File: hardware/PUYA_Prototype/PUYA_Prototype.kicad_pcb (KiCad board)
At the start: 2 copper layers, 19.3 x 31.8 mm, 26 parts, among them J1 SWD, J2 L_Terminal, J3 R_Terminal, SW1 SW_RST, U1 PY32F002AA15M6TU, U2 AP2112K-3.3TRG1

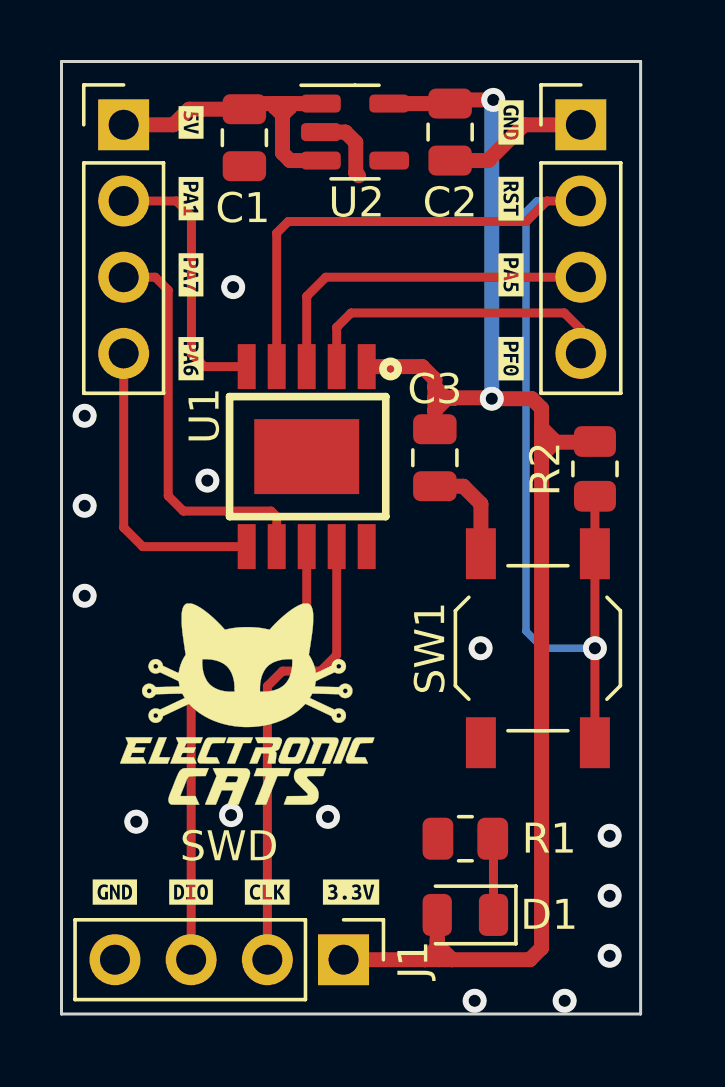
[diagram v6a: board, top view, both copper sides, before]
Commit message: change edge cuts
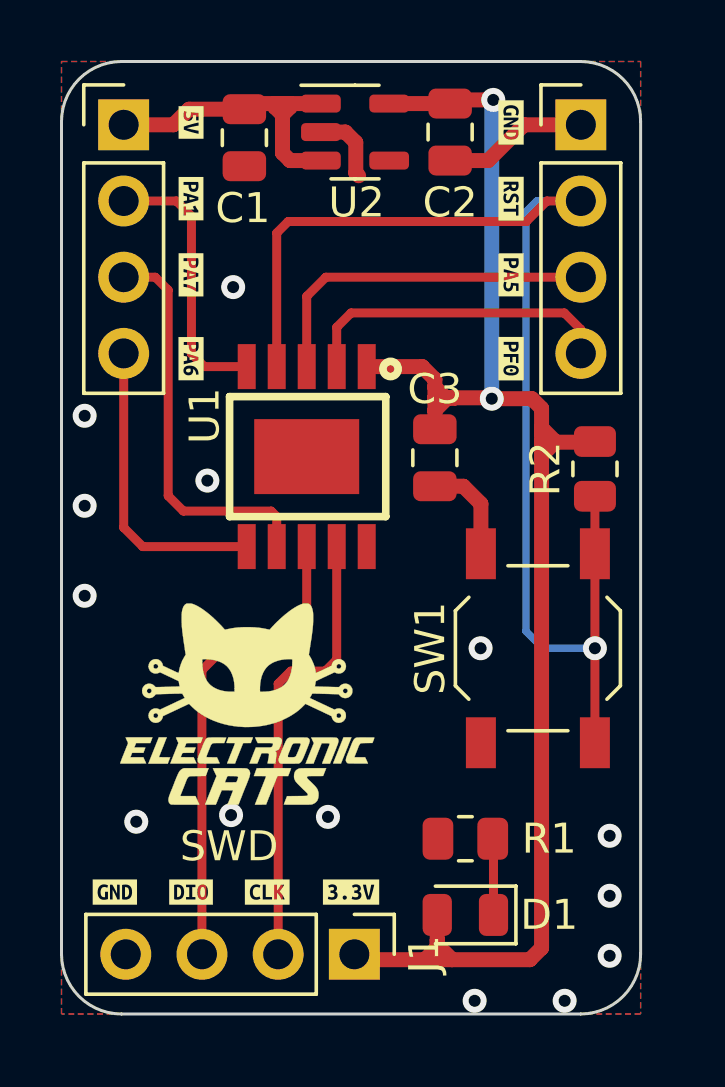
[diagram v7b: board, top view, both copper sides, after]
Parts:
- moved J1 0.40 mm to (119.5, 89.5)
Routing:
- net /SWDIO: track 17.1 -> 16.5 mm
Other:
- outline, holes or cut-outs redrawn
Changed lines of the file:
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@@
   )
   (footprint "Connector_PinHeader_2.54mm:PinHeader_1x04_P2.54mm_Vertical" (layer "F.Cu")
-    (at 119.13 89.63 -90)
+    (at 119.49 89.45 -90)
     (descr "Through hole straight pin header, 1x04, 2.54mm pitch, single row")
     (tags "Through hole pin header THT 1x04 2.54mm single row")
@@
       (stroke (width 0.01) (type solid)) (fill solid) (layer "B.SilkS"))
   )
-  (gr_rect (start 109.728 59.69) (end 129.032 91.44)
-    (stroke (width 0.1) (type default)) (fill none) (layer "Edge.Cuts"))
+  (gr_arc (start 111.728 91.44) (mid 110.313786 90.854214) (end 109.728 89.44)
+    (stroke (width 0.1) (type default)) (layer "Edge.Cuts"))
+  (gr_arc (start 127.032 59.69) (mid 128.446214 60.275786) (end 129.032 61.69)
+    (stroke (width 0.1) (type default)) (layer "Edge.Cuts"))
+  (gr_line (start 127.032 91.44) (end 111.728 91.44)
+    (stroke (width 0.1) (type default)) (layer "Edge.Cuts"))
+  (gr_arc (start 109.728 61.69) (mid 110.313786 60.275786) (end 111.728 59.69)
+    (stroke (width 0.1) (type default)) (layer "Edge.Cuts"))
+  (gr_line (start 111.728 59.69) (end 127.032 59.69)
+    (stroke (width 0.1) (type default)) (layer "Edge.Cuts"))
+  (gr_line (start 129.032 61.69) (end 129.032 89.44)
+    (stroke (width 0.1) (type default)) (layer "Edge.Cuts"))
+  (gr_arc (start 129.032 89.44) (mid 128.446214 90.854214) (end 127.032 91.44)
+    (stroke (width 0.1) (type default)) (layer "Edge.Cuts"))
+  (gr_line (start 109.728 89.44) (end 109.728 61.69)
+    (stroke (width 0.1) (type default)) (layer "Edge.Cuts"))
   (gr_text "Dev Board PY32F" (at 124.46 76.75) (layer "B.SilkS")
     (effects (font (size 1 1) (thickness 0.15)) (justify left bottom mirror))
@@
   (segment (start 122.2525 88.97) (end 122.2525 89.2175) (width 0.5) (layer "F.Cu") (net 3))
   (segment (start 121.75 69.860006) (end 119.901998 69.860006) (width 0.5) (layer "F.Cu") (net 3))
+  (segment (start 119.67 89.63) (end 121.84 89.63) (width 0.5) (layer "F.Cu") (net 3))
   (segment (start 127.4875 72.38) (end 127.51 72.3575) (width 0.5) (layer "F.Cu") (net 3))
   (segment (start 122.86 70.9) (end 122.594 70.9) (width 0.5) (layer "F.Cu") (net 3))
@@
   (segment (start 125.73 72.87) (end 125.73 72.38) (width 0.5) (layer "F.Cu") (net 3))
   (segment (start 126.18 72.35) (end 125.73 71.9) (width 0.5) (layer "F.Cu") (net 3))
+  (segment (start 119.49 89.45) (end 119.67 89.63) (width 0.5) (layer "F.Cu") (net 3))
   (segment (start 125.73 72.38) (end 126.18 72.38) (width 0.5) (layer "F.Cu") (net 3))
   (segment (start 122.174 70.9) (end 122.174 70.54) (width 0.5) (layer "F.Cu") (net 3))
@@
   (segment (start 122.174 70.9) (end 122.86 70.9) (width 0.5) (layer "F.Cu") (net 3))
   (segment (start 122.804 60.97) (end 124.12 60.97) (width 0.5) (layer "F.Cu") (net 3))
-  (segment (start 119.126 89.63) (end 121.84 89.63) (width 0.5) (layer "F.Cu") (net 3))
   (segment (start 122.2525 89.1325) (end 122.75 89.63) (width 0.5) (layer "F.Cu") (net 3))
   (segment (start 122.2525 89.2175) (end 121.84 89.63) (width 0.5) (layer "F.Cu") (net 3))
@@
   (segment (start 124.1025 85.598) (end 124.1275 85.623) (width 0.3) (layer "F.Cu") (net 4))
   (segment (start 124.1275 85.623) (end 124.1275 88.138) (width 0.3) (layer "F.Cu") (net 4))
-  (segment (start 117.094 80.01) (end 116.59 80.514) (width 0.3) (layer "F.Cu") (net 5))
-  (segment (start 118.364 80.01) (end 117.094 80.01) (width 0.3) (layer "F.Cu") (net 5))
-  (segment (start 116.59 89.658) (end 116.586 89.662) (width 0.3) (layer "F.Cu") (net 5))
-  (segment (start 118.902 75.859994) (end 118.902 79.472) (width 0.3) (layer "F.Cu") (net 5))
-  (segment (start 116.59 80.514) (end 116.59 89.658) (width 0.3) (layer "F.Cu") (net 5))
-  (segment (start 118.902 79.472) (end 118.364 80.01) (width 0.3) (layer "F.Cu") (net 5))
-  (segment (start 114.05 79.752) (end 114.05 89.658) (width 0.3) (layer "F.Cu") (net 6))
-  (segment (start 114.05 89.658) (end 114.046 89.662) (width 0.3) (layer "F.Cu") (net 6))
-  (segment (start 117.902002 78.693998) (end 117.348 79.248) (width 0.3) (layer "F.Cu") (net 6))
-  (segment (start 117.348 79.248) (end 114.554 79.248) (width 0.3) (layer "F.Cu") (net 6))
+  (segment (start 116.95 80.43) (end 116.95 89.45) (width 0.3) (layer "F.Cu") (net 5))
+  (segment (start 118.902 79.628) (end 118.52 80.01) (width 0.3) (layer "F.Cu") (net 5))
+  (segment (start 118.52 80.01) (end 117.37 80.01) (width 0.3) (layer "F.Cu") (net 5))
+  (segment (start 117.37 80.01) (end 116.95 80.43) (width 0.3) (layer "F.Cu") (net 5))
+  (segment (start 118.902 75.859994) (end 118.902 79.628) (width 0.3) (layer "F.Cu") (net 5))
+  (segment (start 114.41 79.98) (end 114.41 89.45) (width 0.3) (layer "F.Cu") (net 6))
+  (segment (start 117.902002 75.859994) (end 117.902002 78.927998) (width 0.3) (layer "F.Cu") (net 6))
   (segment (start 117.85 75.911996) (end 117.902002 75.859994) (width 0.3) (layer "F.Cu") (net 6))
-  (segment (start 114.554 79.248) (end 114.05 79.752) (width 0.3) (layer "F.Cu") (net 6))
-  (segment (start 117.902002 75.859994) (end 117.902002 78.693998) (width 0.3) (layer "F.Cu") (net 6))
+  (segment (start 117.38 79.45) (end 114.94 79.45) (width 0.3) (layer "F.Cu") (net 6))
+  (segment (start 117.902002 78.927998) (end 117.38 79.45) (width 0.3) (layer "F.Cu") (net 6))
+  (segment (start 114.94 79.45) (end 114.41 79.98) (width 0.3) (layer "F.Cu") (net 6))
   (segment (start 125.906 64.34) (end 127.04 64.34) (width 0.3) (layer "F.Cu") (net 7))
   (segment (start 125.222 65.024) (end 125.906 64.34) (width 0.3) (layer "F.Cu") (net 7))

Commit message: add "on" serigraphy to D1
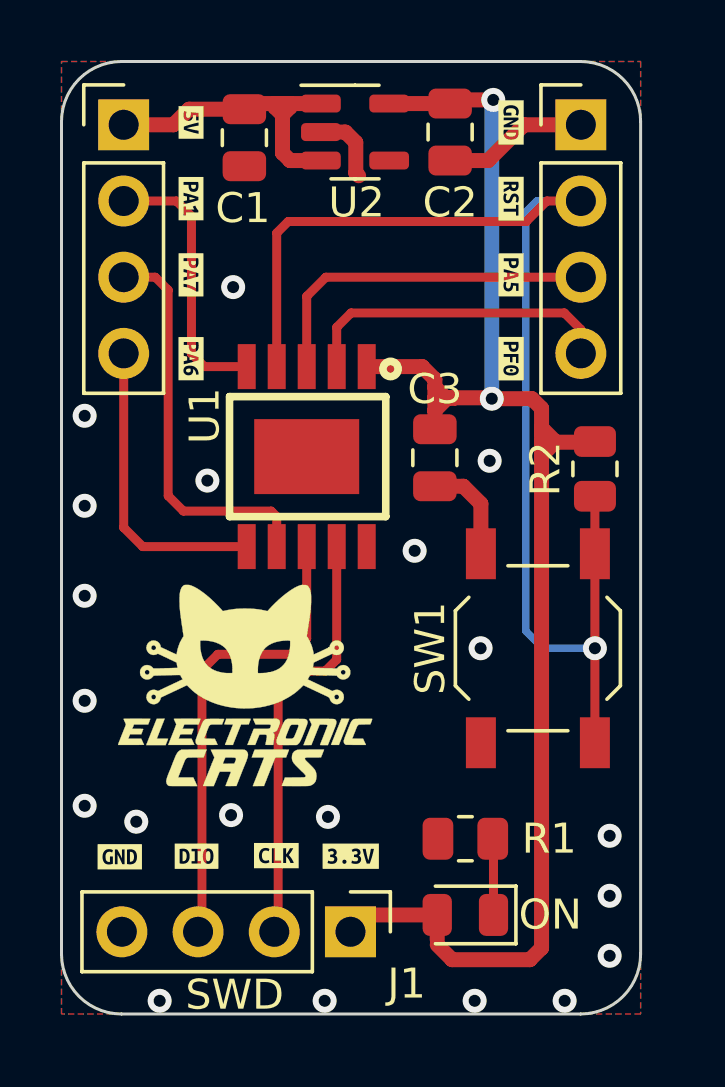
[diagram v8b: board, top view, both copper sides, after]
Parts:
- moved kibuzzard-646D3CBC 1.25 mm to (116.9, 86.2)
- moved kibuzzard-646D3CAB 1.21 mm to (114.2, 86.2)
- moved kibuzzard-646D3CFD 1.20 mm to (119.4, 86.2)
- moved kibuzzard-646D3CA0 1.19 mm to (111.7, 86.2)
- moved J1 0.76 mm to (119.4, 88.7)
- moved G*** 0.62 mm to (115.8, 80.5)
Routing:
- net +3.3V: track 53.4 -> 52.2 mm
- net /SWDIO: track 16.5 -> 15.8 mm
- net /SWCLK: track 15.1 -> 14.4 mm
- net GND: vias 14 -> 20
